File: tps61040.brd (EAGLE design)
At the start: 9.6 x 14.2 mm, 11 parts, among them U1 TPS61040

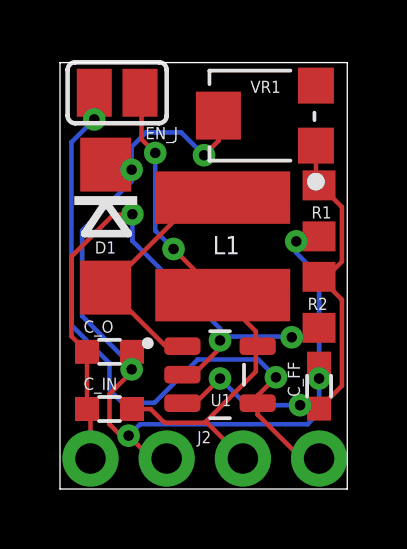
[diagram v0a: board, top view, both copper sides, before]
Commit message: add space for header plastic
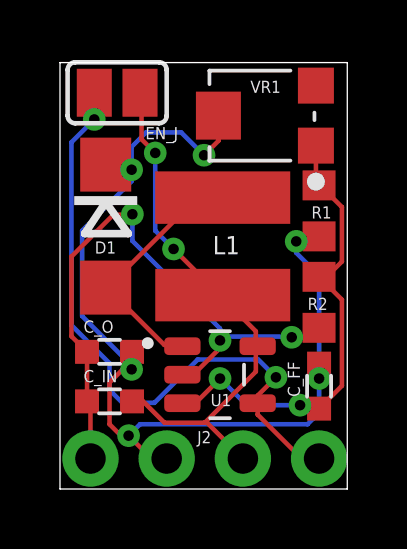
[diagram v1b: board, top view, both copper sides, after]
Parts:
- moved C_IN 0.25 mm to (1.65, 2.92)
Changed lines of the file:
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@@
 <drawing>
 <settings>
-<setting alwaysvectorfont="yes"/>
+<setting alwaysvectorfont="no"/>
 <setting verticaltext="up"/>
 </settings>
@@
 </autorouter>
 <elements>
-<element name="C_IN" library="Passive_Capacitors_rev15a" package="WCAP-CSGP_0603_REFLOW" value="4.7uF" x="1.651" y="2.667" smashed="yes">
-<attribute name="NAME" x="0.786" y="3.305" size="0.4064" layer="25"/>
+<element name="C_IN" library="Passive_Capacitors_rev15a" package="WCAP-CSGP_0603_REFLOW" value="4.7uF" x="1.651" y="2.921" smashed="yes">
+<attribute name="NAME" x="0.786" y="3.559" size="0.4064" layer="25"/>
 </element>
 <element name="C_FF" library="Passive_Capacitors_rev15a" package="WCAP-CSGP_0603_REFLOW" value="22pF" x="8.636" y="3.429" smashed="yes" rot="R90">
@@
 <contactref element="R2" pad="1"/>
 <contactref element="C_O" pad="1"/>
-<wire x1="0.901" y1="2.667" x2="0.901" y2="4.572" width="0.1524" layer="1"/>
+<wire x1="0.901" y1="2.921" x2="0.901" y2="4.572" width="0.1524" layer="1"/>
 <wire x1="0.901" y1="4.572" x2="0.381" y2="5.092" width="0.1524" layer="1"/>
 <wire x1="0.381" y1="5.092" x2="0.381" y2="7.747" width="0.1524" layer="1"/>
@@
 <wire x1="8.3204" y1="5.0574" x2="7.7246" y2="5.0574" width="0.1524" layer="1"/>
 <contactref element="J2" pad="1"/>
-<wire x1="0.901" y1="2.667" x2="1.016" y2="2.552" width="0.1524" layer="1"/>
-<wire x1="1.016" y1="2.552" x2="1.016" y2="1.016" width="0.1524" layer="1"/>
+<wire x1="0.901" y1="2.921" x2="1.016" y2="2.806" width="0.1524" layer="1"/>
+<wire x1="1.016" y1="2.806" x2="1.016" y2="1.016" width="0.1524" layer="1"/>
 </signal>
 <signal name="VOUT">
@@
 <via x="2.3876" y="10.6426" extent="1-16" drill="0.35"/>
 <via x="4.8006" y="11.1252" extent="1-16" drill="0.35"/>
-<wire x1="2.3876" y1="3.9878" x2="2.3876" y2="3.9038875" width="0.1524" layer="1"/>
-<wire x1="2.3876" y1="3.9038875" x2="1.651" y2="3.1672875" width="0.1524" layer="1"/>
-<wire x1="1.651" y1="3.1672875" x2="1.651" y2="2.159" width="0.1524" layer="1"/>
+<wire x1="2.3876" y1="3.9878" x2="2.0905125" y2="3.9878" width="0.1524" layer="1"/>
+<wire x1="2.0905125" y1="3.9878" x2="1.651" y2="3.5482875" width="0.1524" layer="1"/>
+<wire x1="1.651" y1="3.5482875" x2="1.651" y2="2.159" width="0.1524" layer="1"/>
 <wire x1="1.651" y1="2.159" x2="2.032" y2="1.778" width="0.1524" layer="1"/>
 <wire x1="8.636" y1="4.179" x2="8.636" y2="3.683" width="0.1524" layer="1"/>
@@
 <contactref element="C_IN" pad="2"/>
 <contactref element="L1" pad="1"/>
-<wire x1="3.0226" y1="2.667" x2="2.401" y2="2.667" width="0.1524" layer="1"/>
-<wire x1="3.4798" y1="2.2098" x2="3.0226" y2="2.667" width="0.1524" layer="1"/>
+<wire x1="2.7686" y1="2.921" x2="2.401" y2="2.921" width="0.1524" layer="1"/>
+<wire x1="3.4798" y1="2.2098" x2="2.7686" y2="2.921" width="0.1524" layer="1"/>
 <wire x1="6.5278" y1="4.6482" x2="6.5278" y2="3.9116" width="0.1524" layer="1"/>
 <wire x1="6.5278" y1="4.6482" x2="6.589" y2="4.76" width="0.1524" layer="1"/>
